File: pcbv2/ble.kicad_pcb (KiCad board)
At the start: 2 copper layers, 26.8 x 14.5 mm, 19 parts, among them J1 Conn_01x05, J2 Conn_01x09, J3 Conn_01x06, J4 Conn_01x03, J5 Conn_01x01, J6 Conn_01x01, SW1 SW_Push, U1 BMP280

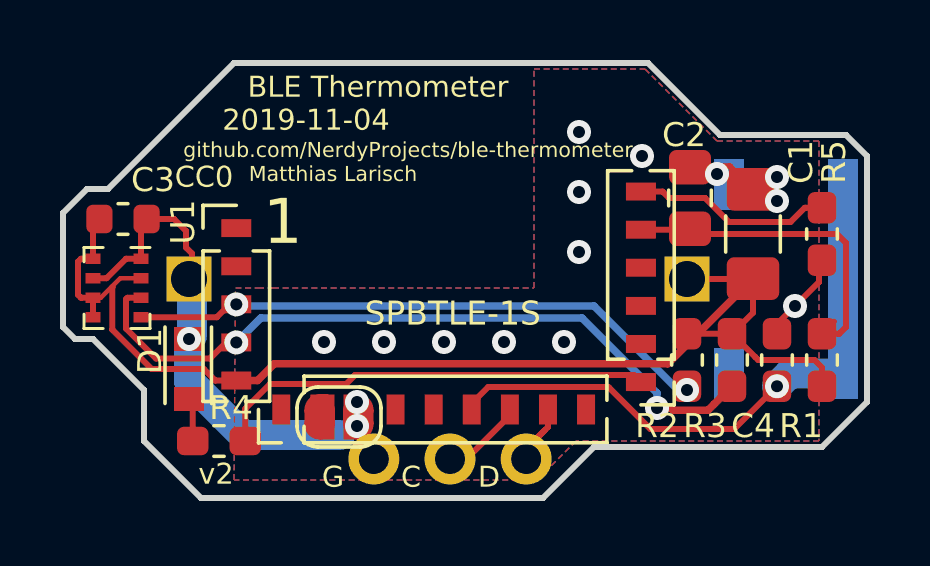
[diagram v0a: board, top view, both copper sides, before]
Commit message: Add second bme capacitor
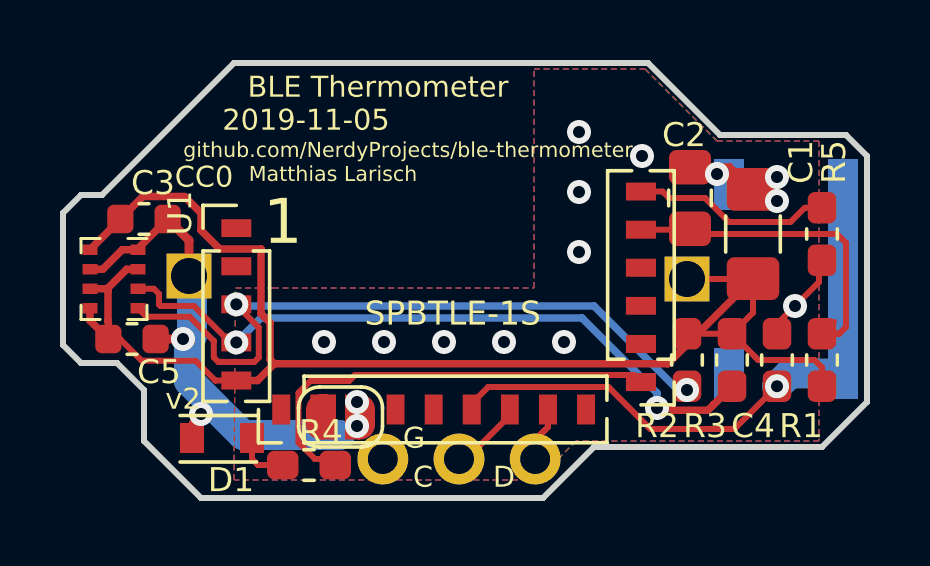
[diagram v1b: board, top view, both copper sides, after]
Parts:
- added C5: 100n, Capacitor_SMD:C_0603_1608Metric, F.Cu at (104.6, 116.7)
- moved R4 3.10 mm to (110.5, 120.9)
- moved D1 2.55 mm to (107.6, 120.0), turned to 0 degrees
- moved C3 0.70 mm to (105.0, 112.7)
- moved U1 0.32 mm to (104.0, 114.7)
- moved J4 0.30 mm to (118.0, 120.7)
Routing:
- net VCC: track 40.9 -> 49.8 mm
- net SCL: track 19.8 -> 23.9 mm
- net SDA: track 24.6 -> 23.3 mm
- net GND: track 21.2 -> 22.4 mm, vias 16 -> 17
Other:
- outline, holes or cut-outs redrawn
- board text added: "2019-11-05"
- board text removed: "2019-11-04"
